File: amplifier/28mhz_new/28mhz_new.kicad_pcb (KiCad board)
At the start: 2 copper layers, 73.2 x 56 mm, 39 parts, among them J1 GPIO, J2 694106301002, M1 RD16HHF1

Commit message: sign pcb and write order :)
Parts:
- moved C1 2.07 mm to (114.8, 98.0), turned to 90 degrees
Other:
- board text added: "'25"
- board text added: "BG"
- board text added: "KQ4TVW"
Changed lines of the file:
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@@
 	(footprint "Capacitor_SMD:C_0805_2012Metric_Pad1.18x1.45mm_HandSolder"
 		(layer "F.Cu")
-		(at 114.75 100.0375 -90)
+		(at 114.75 97.9625 90)
 		(descr "Capacitor SMD 0805 (2012 Metric), square (rectangular) end terminal, IPC_7351 nominal with elongated pad for handsoldering. (Body size source: IPC-SM-782 page 76, https://www.pcb-3d.com/wordpress/wp-content/uploads/ipc-sm-782a_amendment_1_and_2.pdf, https://docs.google.com/spreadsheets/d/1BsfQQcO9C6DZCsRaXUlFlo91Tg2WpOkGARC1WS5S8t0/edit?usp=sharing), generated with kicad-footprint-generator")
 		(tags "capacitor handsolder")
@@
 		)
 		(property "Footprint" "Capacitor_SMD:C_0805_2012Metric_Pad1.18x1.45mm_HandSolder"
-			(at 0 0 -90)
+			(at 0 0 90)
 			(unlocked yes)
 			(layer "F.Fab")
@@
 		)
 		(property "Datasheet" ""
-			(at 0 0 -90)
+			(at 0 0 90)
 			(unlocked yes)
 			(layer "F.Fab")
@@
 		)
 		(property "Description" "600F221FT250XT "
-			(at 0 0 -90)
+			(at 0 0 90)
 			(unlocked yes)
 			(layer "F.Fab")
@@
 		)
 		(property "Sim.Device" "C"
-			(at 0 0 -90)
+			(at 0 0 90)
 			(unlocked yes)
 			(layer "F.Fab")
@@
 		)
 		(property "Sim.Params" "C=220p"
-			(at 0 0 -90)
+			(at 0 0 90)
 			(unlocked yes)
 			(layer "F.Fab")
@@
 		(attr smd)
 		(fp_line
-			(start -0.261252 0.735)
-			(end 0.261252 0.735)
+			(start -0.261252 -0.735)
+			(end 0.261252 -0.735)
 			(stroke
 				(width 0.12)
@@
 		)
 		(fp_line
-			(start -0.261252 -0.735)
-			(end 0.261252 -0.735)
+			(start -0.261252 0.735)
+			(end 0.261252 0.735)
 			(stroke
 				(width 0.12)
@@
 		)
 		(fp_line
-			(start -1.88 0.98)
-			(end -1.88 -0.98)
+			(start 1.88 -0.98)
+			(end 1.88 0.98)
 			(stroke
 				(width 0.05)
@@
 		)
 		(fp_line
-			(start 1.88 0.98)
-			(end -1.88 0.98)
+			(start -1.88 -0.98)
+			(end 1.88 -0.98)
 			(stroke
 				(width 0.05)
@@
 		)
 		(fp_line
-			(start -1.88 -0.98)
-			(end 1.88 -0.98)
+			(start 1.88 0.98)
+			(end -1.88 0.98)
 			(stroke
 				(width 0.05)
@@
 		)
 		(fp_line
-			(start 1.88 -0.98)
-			(end 1.88 0.98)
+			(start -1.88 0.98)
+			(end -1.88 -0.98)
 			(stroke
 				(width 0.05)
@@
 		)
 		(fp_line
-			(start -1 0.625)
-			(end -1 -0.625)
+			(start 1 -0.625)
+			(end 1 0.625)
 			(stroke
 				(width 0.1)
@@
 		)
 		(fp_line
-			(start 1 0.625)
-			(end -1 0.625)
+			(start -1 -0.625)
+			(end 1 -0.625)
 			(stroke
 				(width 0.1)
@@
 		)
 		(fp_line
-			(start -1 -0.625)
-			(end 1 -0.625)
+			(start 1 0.625)
+			(end -1 0.625)
 			(stroke
 				(width 0.1)
@@
 		)
 		(fp_line
-			(start 1 -0.625)
-			(end 1 0.625)
+			(start -1 0.625)
+			(end -1 -0.625)
 			(stroke
 				(width 0.1)
@@
 		)
 		(pad "1" smd roundrect
-			(at -1.0375 0 270)
+			(at -1.0375 0 90)
 			(size 1.175 1.45)
 			(layers "F.Cu" "F.Paste" "F.Mask")
@@
 		)
 		(pad "2" smd roundrect
-			(at 1.0375 0 270)
+			(at 1.0375 0 90)
 			(size 1.175 1.45)
 			(layers "F.Cu" "F.Paste" "F.Mask")
@@
 			(pintype "passive")
 		)
-		(model "B82144A2103K.stp"
+		(model "/home/bean/RadioNotes/amplifier/parts/B82144A2103K/3D/B82144A2103K.stp"
 			(offset
 				(xyz 0 0 0)
@@
 		(layer "Edge.Cuts")
 	)
+	(gr_text "'25"
+		(at 130 68.25 0)
+		(layer "F.SilkS")
+		(effects
+			(font
+				(size 2 2)
+				(thickness 0.3)
+			)
+			(justify left bottom)
+		)
+	)
+	(gr_text "KQ4TVW"
+		(at 129.275 100.75 0)
+		(layer "F.SilkS")
+		(effects
+			(font
+				(size 1.5 1.5)
+				(thickness 0.3)
+			)
+			(justify bottom)
+		)
+	)
+	(gr_text "BG"
+		(at 130.75 65.5 0)
+		(layer "F.Mask")
+		(effects
+			(font
+				(size 2 2)
+				(thickness 0.3)
+			)
+			(justify left bottom)
+		)
+	)
 	(gr_text "USB"

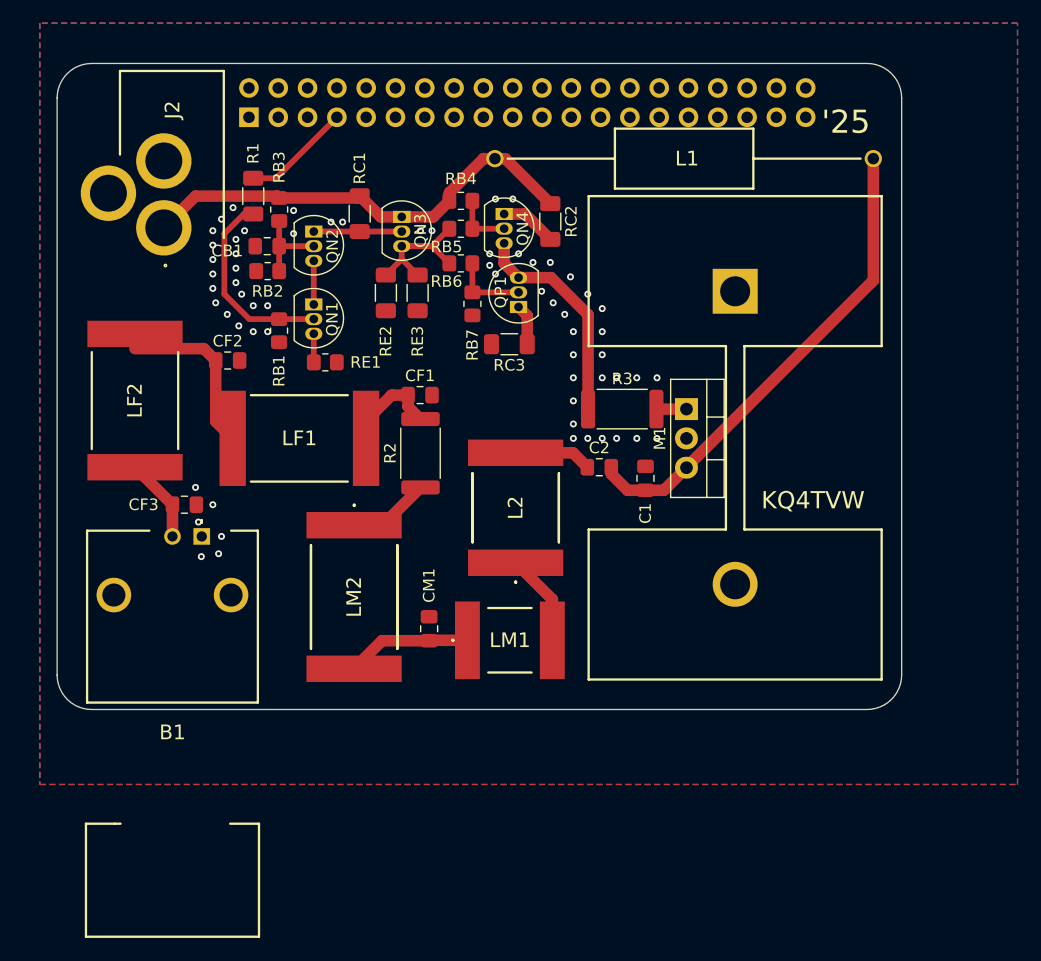
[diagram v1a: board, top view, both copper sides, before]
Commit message: Add ground vias
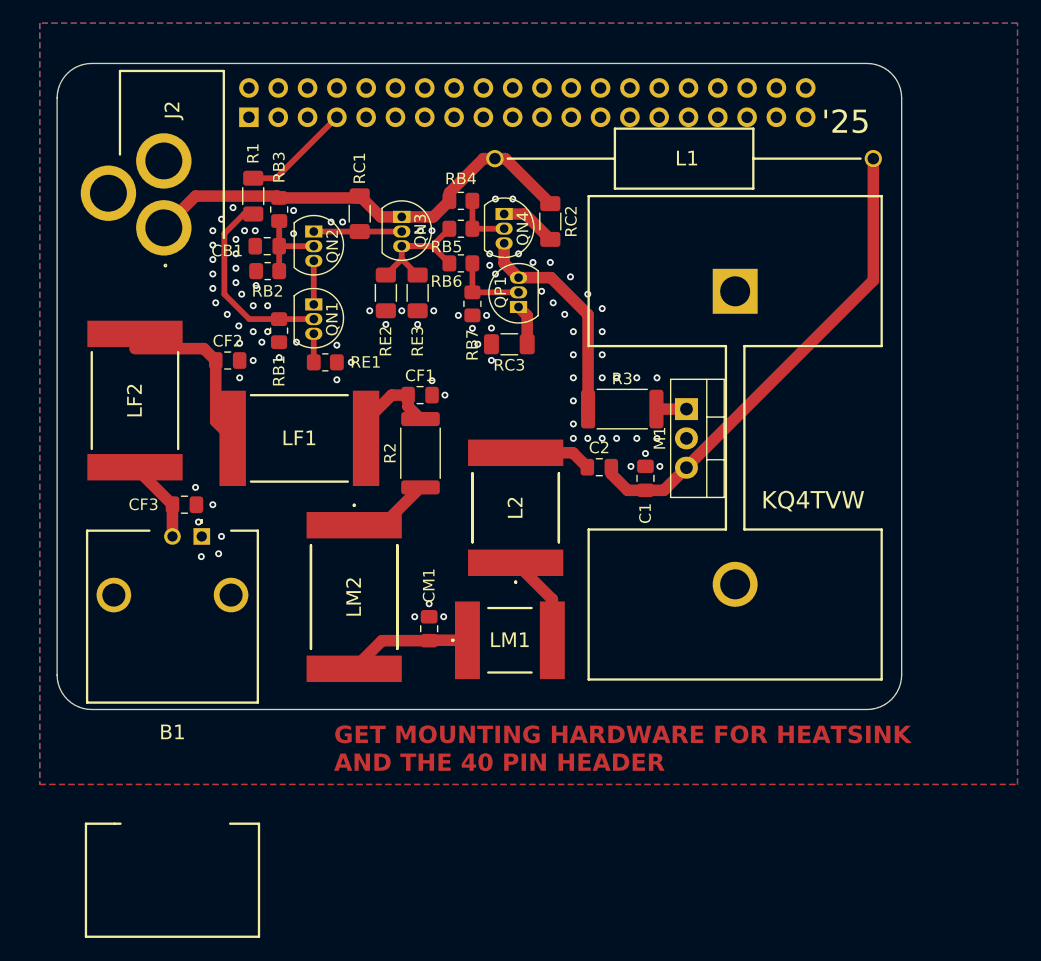
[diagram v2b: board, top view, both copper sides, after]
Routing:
- net 0: vias 63 -> 93
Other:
- board text added: "GET MOUNTING HARDWARE FOR HEATSINK AND THE 40 PIN HEADER"

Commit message: Fix 3904 and 3906 transistor pinout
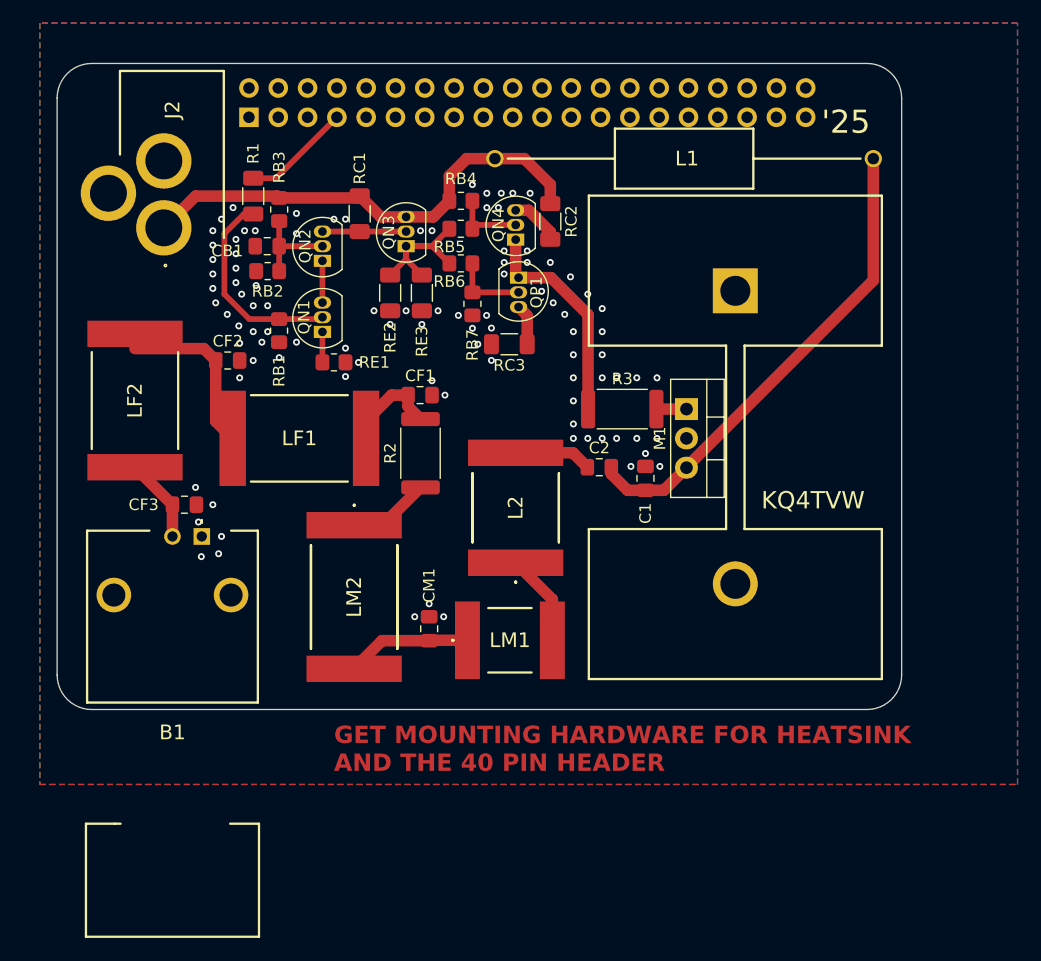
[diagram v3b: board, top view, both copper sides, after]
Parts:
- moved QN2 2.65 mm to (86.8, 79.1), turned to 90 degrees
- moved QN3 2.57 mm to (94.0, 77.8), turned to 90 degrees
- moved QP1 2.54 mm to (103.8, 80.6), turned to -90 degrees
- moved QN1 2.50 mm to (86.8, 85.3), turned to 90 degrees
- moved QN4 2.43 mm to (103.5, 77.3), turned to 90 degrees
- moved RE1 0.75 mm to (87.8, 87.9)
- moved RE2 0.37 mm to (92.6, 81.9)
- moved RE3 0.37 mm to (95.4, 81.9)
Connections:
- QN1 pad 1: Net-(QN1-C) -> Net-(QN1-E)
- QN1 pad 3: Net-(QN1-E) -> Net-(QN1-C)
- QN2 pad 1: Net-(QN2-C) -> Net-(QN1-C)
- QN2 pad 3: Net-(QN1-C) -> Net-(QN2-C)
- QN3 pad 1: /VCC -> Net-(QN3-E)
- QN3 pad 3: Net-(QN3-E) -> /VCC
- QN4 pad 1: Net-(QN4-C) -> Net-(QN4-E)
- QN4 pad 3: Net-(QN4-E) -> Net-(QN4-C)
- QP1 pad 1: Net-(QP1-C) -> Net-(QN4-E)
- QP1 pad 3: Net-(QN4-E) -> Net-(QP1-C)
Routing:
- net /VCC: track 39.8 -> 41.7 mm
- net Net-(QN4-B): track 5.24 -> 6.38 mm
- net Net-(QN3-E): track 14.5 -> 15.6 mm
- net Net-(QN2-C): track 7.62 -> 6.88 mm
- net Net-(QN2-B): track 7.25 -> 8.00 mm
- net Net-(QN1-B): track 17.2 -> 17.9 mm
- net 0: vias 93 -> 98

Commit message: Add mounting holes
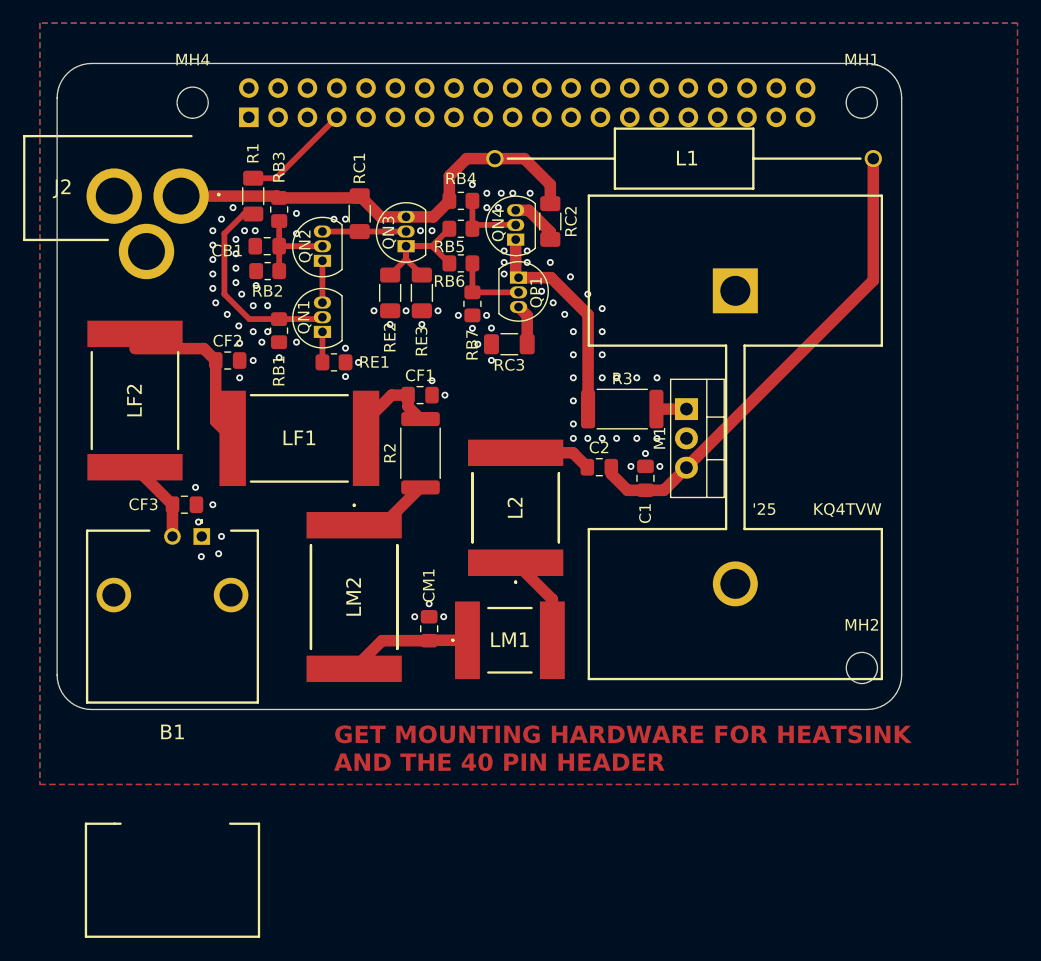
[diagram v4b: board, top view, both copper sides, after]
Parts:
- added MH1: MountingHole_2.7mm_M2.5, MountingHole:MountingHole_2.7mm_M2.5, F.Cu at (133.5, 65.4)
- added MH2: MountingHole_2.7mm_M2.5, MountingHole:MountingHole_2.7mm_M2.5, F.Cu at (133.5, 114.4)
- added MH4: MountingHole_2.7mm_M2.5, MountingHole:MountingHole_2.7mm_M2.5, F.Cu at (75.5, 65.4)
- moved J2 16.8 mm to (60.9, 77.3), turned to 0 degrees
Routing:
- net /VCC: track 41.7 -> 39.0 mm

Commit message: Add places for bias resistors for RD16HHF1
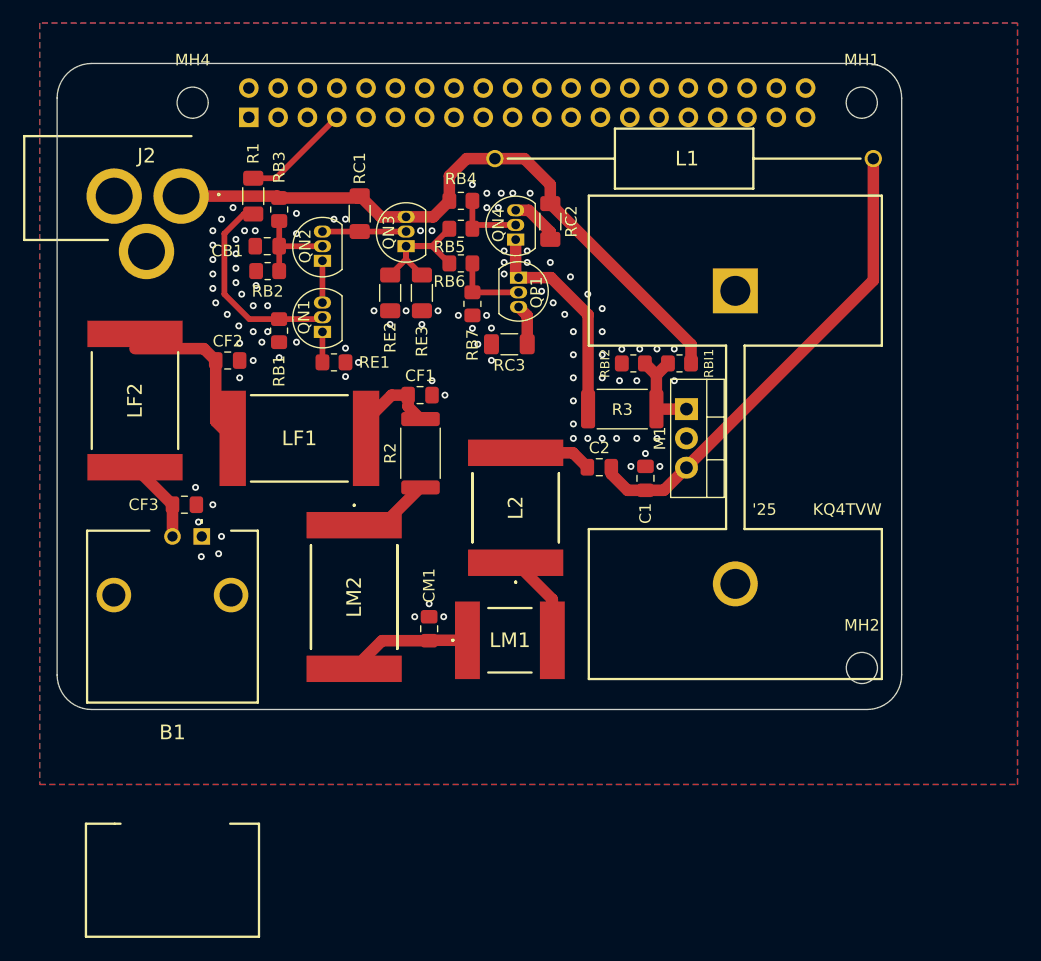
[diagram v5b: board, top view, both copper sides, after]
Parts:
- added RBI1: R_0805_2012Metric_Pad1.20x1.40mm_HandSolder, Resistor_SMD:R_0805_2012Metric_Pad1.20x1.40mm_HandSolder, F.Cu at (117.7, 88.0)
- added RBI2: R_0805_2012Metric_Pad1.20x1.40mm_HandSolder, Resistor_SMD:R_0805_2012Metric_Pad1.20x1.40mm_HandSolder, F.Cu at (113.7, 88.0)
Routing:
- net /VCC: track 39.0 -> 57.9 mm
- net Net-(M1-G): track 2.61 -> 8.39 mm
- net 0: vias 98 -> 102
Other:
- board text removed: "GET MOUNTING HARDWARE FOR HEATSINK AND THE 40 PIN HEADER"

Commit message: Generate Gerber and drill files again
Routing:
- net Net-(M1-D): track 42.0 -> 45.1 mm
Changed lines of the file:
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@@
 			(plot_on_all_layers_selection 0x0000000_00000000)
 			(disableapertmacros no)
-			(usegerberextensions no)
+			(usegerberextensions yes)
 			(usegerberattributes yes)
 			(usegerberadvancedattributes yes)
@@
 			(plotinvisibletext no)
 			(sketchpadsonfab no)
-			(subtractmaskfromsilk no)
+			(subtractmaskfromsilk yes)
 			(outputformat 1)
 			(mirror no)
-			(drillshape 1)
+			(drillshape 0)
 			(scaleselection 1)
 			(outputdirectory "")
@@
 	(segment
 		(start 134.5 70.25)
-		(end 134.5 80.805)
+		(end 134.5 86.25)
 		(width 1)
 		(layer "F.Cu")
@@
 	)
 	(segment
-		(start 134.5 80.805)
+		(start 123.75 97)
 		(end 118.305 97)
 		(width 1)
 		(layer "F.Cu")
+		(net 2)
+	)
+	(segment
+		(start 134.5 86.25)
+		(end 123.75 97)
+		(width 1)
+		(layer "F.Cu")
